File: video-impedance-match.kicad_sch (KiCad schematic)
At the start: 7 parts

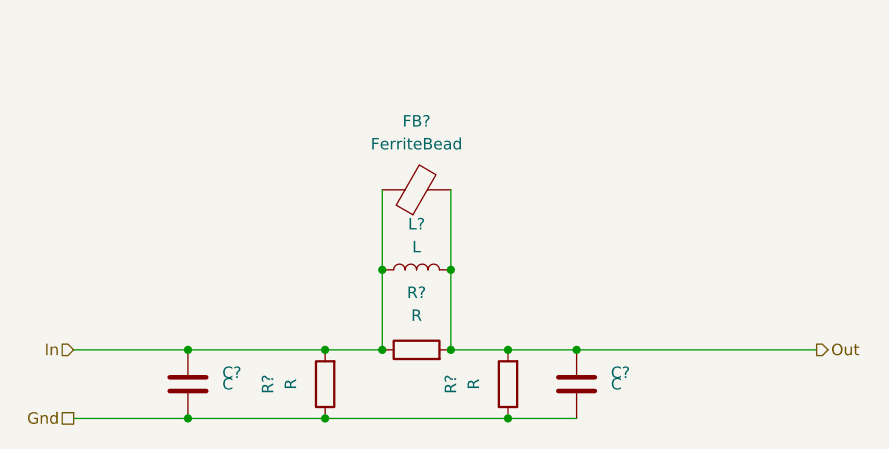
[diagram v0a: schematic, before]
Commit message: Jamma symbol and footprint added. Power supply caps added to schematic.
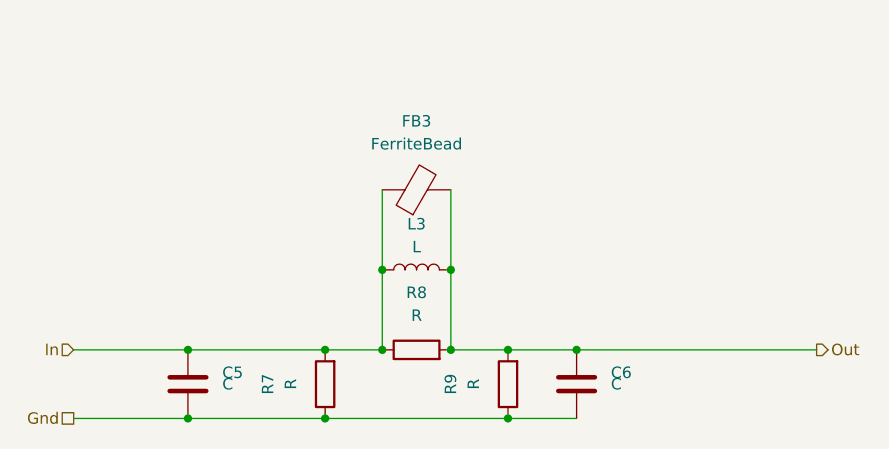
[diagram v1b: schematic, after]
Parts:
- gave numbers to parts that had none: 7
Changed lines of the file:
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@@
   (symbol (lib_id "Device:L") (at 114.3 72.39 90)
     (in_bom yes) (on_board yes)
-    (property "Reference" "L?" (id 0) (at 114.3 67.31 90))
+    (property "Reference" "L3" (id 0) (at 114.3 67.31 90))
     (property "Value" "L" (id 1) (at 114.3 69.85 90))
     (property "Footprint" "" (id 2) (at 114.3 72.39 0)
@@
   (symbol (lib_id "Device:R") (at 104.14 85.09 180)
     (in_bom yes) (on_board yes)
-    (property "Reference" "R?" (id 0) (at 97.79 85.09 90))
+    (property "Reference" "R7" (id 0) (at 97.79 85.09 90))
     (property "Value" "R" (id 1) (at 100.33 85.09 90))
     (property "Footprint" "" (id 2) (at 105.918 85.09 90)
@@
   (symbol (lib_id "Device:R") (at 114.3 81.28 90)
     (in_bom yes) (on_board yes)
-    (property "Reference" "R?" (id 0) (at 114.3 74.93 90))
+    (property "Reference" "R8" (id 0) (at 114.3 74.93 90))
     (property "Value" "R" (id 1) (at 114.3 77.47 90))
     (property "Footprint" "" (id 2) (at 114.3 83.058 90)
@@
   (symbol (lib_id "Device:R") (at 124.46 85.09 180)
     (in_bom yes) (on_board yes)
-    (property "Reference" "R?" (id 0) (at 118.11 85.09 90))
+    (property "Reference" "R9" (id 0) (at 118.11 85.09 90))
     (property "Value" "R" (id 1) (at 120.65 85.09 90))
     (property "Footprint" "" (id 2) (at 126.238 85.09 90)
@@
   (symbol (lib_id "Device:C") (at 88.9 85.09 0)
     (in_bom yes) (on_board yes)
-    (property "Reference" "C?" (id 0) (at 92.71 83.82 0)
+    (property "Reference" "C5" (id 0) (at 92.71 83.82 0)
       (effects (font (size 1.27 1.27)) (justify left))
     )
@@
   (symbol (lib_id "Device:C") (at 132.08 85.09 0)
     (in_bom yes) (on_board yes)
-    (property "Reference" "C?" (id 0) (at 135.89 83.82 0)
+    (property "Reference" "C6" (id 0) (at 135.89 83.82 0)
       (effects (font (size 1.27 1.27)) (justify left))
     )
@@
   (symbol (lib_id "Device:FerriteBead") (at 114.3 63.5 90)
     (in_bom yes) (on_board yes)
-    (property "Reference" "FB?" (id 0) (at 114.3 55.88 90))
+    (property "Reference" "FB3" (id 0) (at 114.3 55.88 90))
     (property "Value" "FerriteBead" (id 1) (at 114.3 58.42 90))
     (property "Footprint" "" (id 2) (at 114.3 65.278 90)

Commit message: Progress with labels and footprints
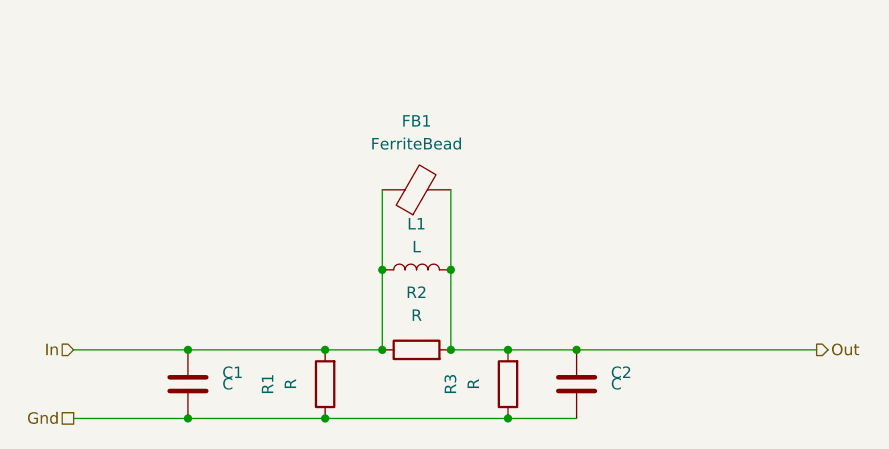
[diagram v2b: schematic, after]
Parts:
- C1: renamed from C5; footprint (none) -> Capacitor_SMD:C_0603_1608Metric
- C2: renamed from C6; footprint (none) -> Capacitor_SMD:C_0603_1608Metric
- FB1: renamed from FB3; footprint (none) -> Resistor_SMD:R_0603_1608Metric
- L1: renamed from L3; footprint (none) -> Resistor_SMD:R_1210_3225Metric
- R1: renamed from R7; footprint (none) -> Resistor_SMD:R_0603_1608Metric
- R2: renamed from R8; footprint (none) -> Resistor_SMD:R_0603_1608Metric
- R3: renamed from R9; footprint (none) -> Resistor_SMD:R_0603_1608Metric
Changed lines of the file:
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@@
   (symbol (lib_id "Device:L") (at 114.3 72.39 90)
     (in_bom yes) (on_board yes)
-    (property "Reference" "L3" (id 0) (at 114.3 67.31 90))
+    (property "Reference" "L1" (id 0) (at 114.3 67.31 90))
     (property "Value" "L" (id 1) (at 114.3 69.85 90))
-    (property "Footprint" "" (id 2) (at 114.3 72.39 0)
+    (property "Footprint" "Resistor_SMD:R_1210_3225Metric" (id 2) (at 114.3 72.39 0)
       (effects (font (size 1.27 1.27)) hide)
     )
@@
   (symbol (lib_id "Device:R") (at 104.14 85.09 180)
     (in_bom yes) (on_board yes)
-    (property "Reference" "R7" (id 0) (at 97.79 85.09 90))
+    (property "Reference" "R1" (id 0) (at 97.79 85.09 90))
     (property "Value" "R" (id 1) (at 100.33 85.09 90))
-    (property "Footprint" "" (id 2) (at 105.918 85.09 90)
+    (property "Footprint" "Resistor_SMD:R_0603_1608Metric" (id 2) (at 105.918 85.09 90)
       (effects (font (size 1.27 1.27)) hide)
     )
@@
   (symbol (lib_id "Device:R") (at 114.3 81.28 90)
     (in_bom yes) (on_board yes)
-    (property "Reference" "R8" (id 0) (at 114.3 74.93 90))
+    (property "Reference" "R2" (id 0) (at 114.3 74.93 90))
     (property "Value" "R" (id 1) (at 114.3 77.47 90))
-    (property "Footprint" "" (id 2) (at 114.3 83.058 90)
+    (property "Footprint" "Resistor_SMD:R_0603_1608Metric" (id 2) (at 114.3 83.058 90)
       (effects (font (size 1.27 1.27)) hide)
     )
@@
   (symbol (lib_id "Device:R") (at 124.46 85.09 180)
     (in_bom yes) (on_board yes)
-    (property "Reference" "R9" (id 0) (at 118.11 85.09 90))
+    (property "Reference" "R3" (id 0) (at 118.11 85.09 90))
     (property "Value" "R" (id 1) (at 120.65 85.09 90))
-    (property "Footprint" "" (id 2) (at 126.238 85.09 90)
+    (property "Footprint" "Resistor_SMD:R_0603_1608Metric" (id 2) (at 126.238 85.09 90)
       (effects (font (size 1.27 1.27)) hide)
     )
@@
   (symbol (lib_id "Device:C") (at 88.9 85.09 0)
     (in_bom yes) (on_board yes)
-    (property "Reference" "C5" (id 0) (at 92.71 83.82 0)
+    (property "Reference" "C1" (id 0) (at 92.71 83.82 0)
       (effects (font (size 1.27 1.27)) (justify left))
     )
@@
       (effects (font (size 1.27 1.27)) (justify left))
     )
-    (property "Footprint" "" (id 2) (at 89.8652 88.9 0)
+    (property "Footprint" "Capacitor_SMD:C_0603_1608Metric" (id 2) (at 89.8652 88.9 0)
       (effects (font (size 1.27 1.27)) hide)
     )
@@
   (symbol (lib_id "Device:C") (at 132.08 85.09 0)
     (in_bom yes) (on_board yes)
-    (property "Reference" "C6" (id 0) (at 135.89 83.82 0)
+    (property "Reference" "C2" (id 0) (at 135.89 83.82 0)
       (effects (font (size 1.27 1.27)) (justify left))
     )
@@
       (effects (font (size 1.27 1.27)) (justify left))
     )
-    (property "Footprint" "" (id 2) (at 133.0452 88.9 0)
+    (property "Footprint" "Capacitor_SMD:C_0603_1608Metric" (id 2) (at 133.0452 88.9 0)
       (effects (font (size 1.27 1.27)) hide)
     )
@@
   (symbol (lib_id "Device:FerriteBead") (at 114.3 63.5 90)
     (in_bom yes) (on_board yes)
-    (property "Reference" "FB3" (id 0) (at 114.3 55.88 90))
+    (property "Reference" "FB1" (id 0) (at 114.3 55.88 90))
     (property "Value" "FerriteBead" (id 1) (at 114.3 58.42 90))
-    (property "Footprint" "" (id 2) (at 114.3 65.278 90)
+    (property "Footprint" "Resistor_SMD:R_0603_1608Metric" (id 2) (at 114.3 65.278 90)
       (effects (font (size 1.27 1.27)) hide)
     )

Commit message: Added more power bypassing capacitors to 5v and 12v supplies.
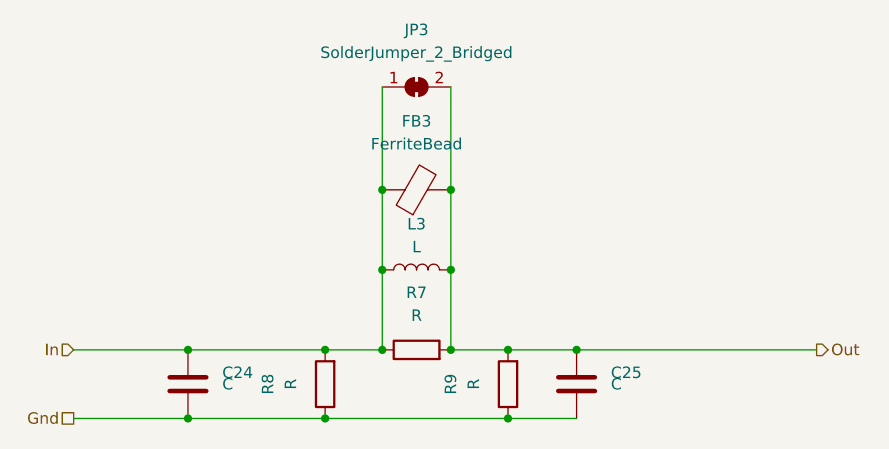
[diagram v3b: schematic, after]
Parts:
- added JP3: SolderJumper_2_Bridged, Jumper:SolderJumper-2_P1.3mm_Bridged_Pad1.0x1.5mm, symbol Jumper:SolderJumper_2_Bridged
- renumbered C1 to C24, C2 to C25, FB1 to FB3, L1 to L3, R2 to R7, R1 to R8, R3 to R9
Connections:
- net In: now also JP3.1 (A)
- net Out: now also JP3.2 (B)
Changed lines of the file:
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@@
   (junction (at 104.14 81.28) (diameter 0.9144) (color 0 0 0 0))
   (junction (at 104.14 88.9) (diameter 0.9144) (color 0 0 0 0))
+  (junction (at 110.49 63.5) (diameter 0.9144) (color 0 0 0 0))
   (junction (at 110.49 72.39) (diameter 0.9144) (color 0 0 0 0))
   (junction (at 110.49 81.28) (diameter 0.9144) (color 0 0 0 0))
+  (junction (at 118.11 63.5) (diameter 0.9144) (color 0 0 0 0))
   (junction (at 118.11 72.39) (diameter 0.9144) (color 0 0 0 0))
   (junction (at 118.11 81.28) (diameter 0.9144) (color 0 0 0 0))
@@
     (stroke (width 0) (type solid) (color 0 0 0 0))
   )
+  (wire (pts (xy 110.49 52.07) (xy 110.49 63.5))
+    (stroke (width 0) (type solid) (color 0 0 0 0))
+  )
   (wire (pts (xy 110.49 63.5) (xy 110.49 72.39))
     (stroke (width 0) (type solid) (color 0 0 0 0))
   )
   (wire (pts (xy 110.49 72.39) (xy 110.49 81.28))
+    (stroke (width 0) (type solid) (color 0 0 0 0))
+  )
+  (wire (pts (xy 118.11 52.07) (xy 118.11 63.5))
     (stroke (width 0) (type solid) (color 0 0 0 0))
   )
@@
   (symbol (lib_id "Device:L") (at 114.3 72.39 90)
     (in_bom yes) (on_board yes)
-    (property "Reference" "L1" (id 0) (at 114.3 67.31 90))
+    (property "Reference" "L3" (id 0) (at 114.3 67.31 90))
     (property "Value" "L" (id 1) (at 114.3 69.85 90))
     (property "Footprint" "Resistor_SMD:R_1210_3225Metric" (id 2) (at 114.3 72.39 0)
@@
   (symbol (lib_id "Device:R") (at 104.14 85.09 180)
     (in_bom yes) (on_board yes)
-    (property "Reference" "R1" (id 0) (at 97.79 85.09 90))
+    (property "Reference" "R8" (id 0) (at 97.79 85.09 90))
     (property "Value" "R" (id 1) (at 100.33 85.09 90))
     (property "Footprint" "Resistor_SMD:R_0603_1608Metric" (id 2) (at 105.918 85.09 90)
@@
   (symbol (lib_id "Device:R") (at 114.3 81.28 90)
     (in_bom yes) (on_board yes)
-    (property "Reference" "R2" (id 0) (at 114.3 74.93 90))
+    (property "Reference" "R7" (id 0) (at 114.3 74.93 90))
     (property "Value" "R" (id 1) (at 114.3 77.47 90))
     (property "Footprint" "Resistor_SMD:R_0603_1608Metric" (id 2) (at 114.3 83.058 90)
@@
   (symbol (lib_id "Device:R") (at 124.46 85.09 180)
     (in_bom yes) (on_board yes)
-    (property "Reference" "R3" (id 0) (at 118.11 85.09 90))
+    (property "Reference" "R9" (id 0) (at 118.11 85.09 90))
     (property "Value" "R" (id 1) (at 120.65 85.09 90))
     (property "Footprint" "Resistor_SMD:R_0603_1608Metric" (id 2) (at 126.238 85.09 90)
@@
     )
   )
+  (symbol (lib_id "Jumper:SolderJumper_2_Bridged") (at 114.3 52.07 0)
+    (in_bom yes) (on_board yes)
+    (property "Reference" "JP3" (id 0) (at 114.3 45.72 0))
+    (property "Value" "SolderJumper_2_Bridged" (id 1) (at 114.3 48.26 0))
+    (property "Footprint" "Jumper:SolderJumper-2_P1.3mm_Bridged_Pad1.0x1.5mm" (id 2) (at 114.3 52.07 0)
+      (effects (font (size 1.27 1.27)) hide)
+    )
+    (property "Datasheet" "~" (id 3) (at 114.3 52.07 0)
+      (effects (font (size 1.27 1.27)) hide)
+    )
+  )
   (symbol (lib_id "Device:C") (at 88.9 85.09 0)
     (in_bom yes) (on_board yes)
-    (property "Reference" "C1" (id 0) (at 92.71 83.82 0)
+    (property "Reference" "C24" (id 0) (at 92.71 83.82 0)
       (effects (font (size 1.27 1.27)) (justify left))
     )
@@
   (symbol (lib_id "Device:C") (at 132.08 85.09 0)
     (in_bom yes) (on_board yes)
-    (property "Reference" "C2" (id 0) (at 135.89 83.82 0)
+    (property "Reference" "C25" (id 0) (at 135.89 83.82 0)
       (effects (font (size 1.27 1.27)) (justify left))
     )
@@
   (symbol (lib_id "Device:FerriteBead") (at 114.3 63.5 90)
     (in_bom yes) (on_board yes)
-    (property "Reference" "FB1" (id 0) (at 114.3 55.88 90))
+    (property "Reference" "FB3" (id 0) (at 114.3 55.88 90))
     (property "Value" "FerriteBead" (id 1) (at 114.3 58.42 90))
     (property "Footprint" "Resistor_SMD:R_0603_1608Metric" (id 2) (at 114.3 65.278 90)

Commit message: Added test points/breakout points for video filter input and output
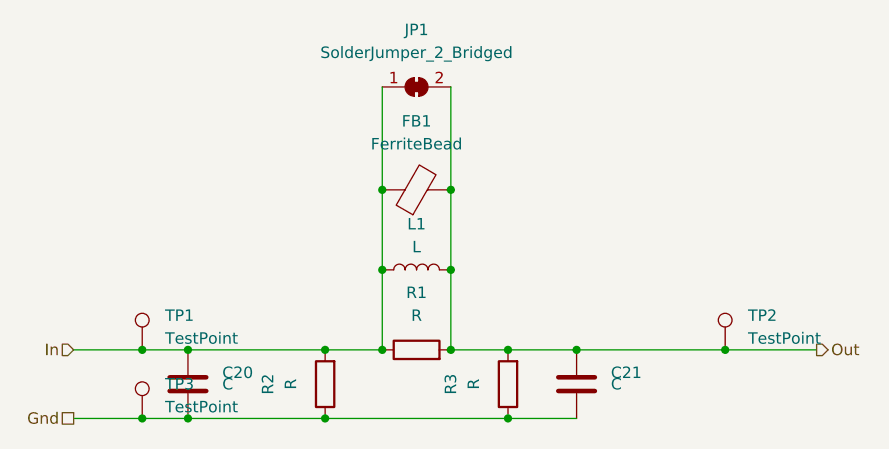
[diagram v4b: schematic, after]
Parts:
- added TP1, TP2, TP3: TestPoint, Connector_PinHeader_2.54mm:PinHeader_1x01_P2.54mm_Vertical, symbol Connector:TestPoint
- renumbered C24 to C20, C25 to C21, FB3 to FB1, JP3 to JP1, L3 to L1, R7 to R1, R8 to R2, R9 to R3
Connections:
- net Gnd: now also TP3.1
- net In: now also TP1.1
- net Out: now also TP2.1
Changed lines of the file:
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@@
   (page 0 4)
   (paper "A4")
+  (junction (at 83.82 81.28) (diameter 0.9144) (color 0 0 0 0))
+  (junction (at 83.82 88.9) (diameter 0.9144) (color 0 0 0 0))
   (junction (at 88.9 81.28) (diameter 0.9144) (color 0 0 0 0))
   (junction (at 88.9 88.9) (diameter 0.9144) (color 0 0 0 0))
@@
   (junction (at 124.46 88.9) (diameter 0.9144) (color 0 0 0 0))
   (junction (at 132.08 81.28) (diameter 0.9144) (color 0 0 0 0))
-  (wire (pts (xy 76.2 81.28) (xy 88.9 81.28))
-    (stroke (width 0) (type solid) (color 0 0 0 0))
-  )
-  (wire (pts (xy 76.2 88.9) (xy 88.9 88.9))
+  (junction (at 148.59 81.28) (diameter 0.9144) (color 0 0 0 0))
+  (wire (pts (xy 76.2 81.28) (xy 83.82 81.28))
+    (stroke (width 0) (type solid) (color 0 0 0 0))
+  )
+  (wire (pts (xy 76.2 88.9) (xy 83.82 88.9))
+    (stroke (width 0) (type solid) (color 0 0 0 0))
+  )
+  (wire (pts (xy 83.82 81.28) (xy 88.9 81.28))
+    (stroke (width 0) (type solid) (color 0 0 0 0))
+  )
+  (wire (pts (xy 83.82 88.9) (xy 88.9 88.9))
     (stroke (width 0) (type solid) (color 0 0 0 0))
   )
@@
     (stroke (width 0) (type solid) (color 0 0 0 0))
   )
-  (wire (pts (xy 132.08 81.28) (xy 158.75 81.28))
+  (wire (pts (xy 132.08 81.28) (xy 148.59 81.28))
+    (stroke (width 0) (type solid) (color 0 0 0 0))
+  )
+  (wire (pts (xy 148.59 81.28) (xy 158.75 81.28))
     (stroke (width 0) (type solid) (color 0 0 0 0))
   )
@@
     (effects (font (size 1.27 1.27)) (justify left))
   )
+  (symbol (lib_id "Connector:TestPoint") (at 83.82 81.28 0)
+    (in_bom yes) (on_board yes)
+    (property "Reference" "TP1" (id 0) (at 86.36 77.47 0)
+      (effects (font (size 1.27 1.27)) (justify left))
+    )
+    (property "Value" "TestPoint" (id 1) (at 86.36 80.01 0)
+      (effects (font (size 1.27 1.27)) (justify left))
+    )
+    (property "Footprint" "Connector_PinHeader_2.54mm:PinHeader_1x01_P2.54mm_Vertical" (id 2) (at 88.9 81.28 0)
+      (effects (font (size 1.27 1.27)) hide)
+    )
+    (property "Datasheet" "~" (id 3) (at 88.9 81.28 0)
+      (effects (font (size 1.27 1.27)) hide)
+    )
+  )
+  (symbol (lib_id "Connector:TestPoint") (at 83.82 88.9 0)
+    (in_bom yes) (on_board yes)
+    (property "Reference" "TP3" (id 0) (at 86.36 85.09 0)
+      (effects (font (size 1.27 1.27)) (justify left))
+    )
+    (property "Value" "TestPoint" (id 1) (at 86.36 87.63 0)
+      (effects (font (size 1.27 1.27)) (justify left))
+    )
+    (property "Footprint" "Connector_PinHeader_2.54mm:PinHeader_1x01_P2.54mm_Vertical" (id 2) (at 88.9 88.9 0)
+      (effects (font (size 1.27 1.27)) hide)
+    )
+    (property "Datasheet" "~" (id 3) (at 88.9 88.9 0)
+      (effects (font (size 1.27 1.27)) hide)
+    )
+  )
+  (symbol (lib_id "Connector:TestPoint") (at 148.59 81.28 0)
+    (in_bom yes) (on_board yes)
+    (property "Reference" "TP2" (id 0) (at 151.13 77.47 0)
+      (effects (font (size 1.27 1.27)) (justify left))
+    )
+    (property "Value" "TestPoint" (id 1) (at 151.13 80.01 0)
+      (effects (font (size 1.27 1.27)) (justify left))
+    )
+    (property "Footprint" "Connector_PinHeader_2.54mm:PinHeader_1x01_P2.54mm_Vertical" (id 2) (at 153.67 81.28 0)
+      (effects (font (size 1.27 1.27)) hide)
+    )
+    (property "Datasheet" "~" (id 3) (at 153.67 81.28 0)
+      (effects (font (size 1.27 1.27)) hide)
+    )
+  )
   (symbol (lib_id "Device:L") (at 114.3 72.39 90)
     (in_bom yes) (on_board yes)
-    (property "Reference" "L3" (id 0) (at 114.3 67.31 90))
+    (property "Reference" "L1" (id 0) (at 114.3 67.31 90))
     (property "Value" "L" (id 1) (at 114.3 69.85 90))
     (property "Footprint" "Resistor_SMD:R_1210_3225Metric" (id 2) (at 114.3 72.39 0)
@@
   (symbol (lib_id "Device:R") (at 104.14 85.09 180)
     (in_bom yes) (on_board yes)
-    (property "Reference" "R8" (id 0) (at 97.79 85.09 90))
+    (property "Reference" "R2" (id 0) (at 97.79 85.09 90))
     (property "Value" "R" (id 1) (at 100.33 85.09 90))
     (property "Footprint" "Resistor_SMD:R_0603_1608Metric" (id 2) (at 105.918 85.09 90)
@@
   (symbol (lib_id "Device:R") (at 114.3 81.28 90)
     (in_bom yes) (on_board yes)
-    (property "Reference" "R7" (id 0) (at 114.3 74.93 90))
+    (property "Reference" "R1" (id 0) (at 114.3 74.93 90))
     (property "Value" "R" (id 1) (at 114.3 77.47 90))
     (property "Footprint" "Resistor_SMD:R_0603_1608Metric" (id 2) (at 114.3 83.058 90)
@@
   (symbol (lib_id "Device:R") (at 124.46 85.09 180)
     (in_bom yes) (on_board yes)
-    (property "Reference" "R9" (id 0) (at 118.11 85.09 90))
+    (property "Reference" "R3" (id 0) (at 118.11 85.09 90))
     (property "Value" "R" (id 1) (at 120.65 85.09 90))
     (property "Footprint" "Resistor_SMD:R_0603_1608Metric" (id 2) (at 126.238 85.09 90)
@@
   (symbol (lib_id "Jumper:SolderJumper_2_Bridged") (at 114.3 52.07 0)
     (in_bom yes) (on_board yes)
-    (property "Reference" "JP3" (id 0) (at 114.3 45.72 0))
+    (property "Reference" "JP1" (id 0) (at 114.3 45.72 0))
     (property "Value" "SolderJumper_2_Bridged" (id 1) (at 114.3 48.26 0))
     (property "Footprint" "Jumper:SolderJumper-2_P1.3mm_Bridged_Pad1.0x1.5mm" (id 2) (at 114.3 52.07 0)
@@
   (symbol (lib_id "Device:C") (at 88.9 85.09 0)
     (in_bom yes) (on_board yes)
-    (property "Reference" "C24" (id 0) (at 92.71 83.82 0)
+    (property "Reference" "C20" (id 0) (at 92.71 83.82 0)
       (effects (font (size 1.27 1.27)) (justify left))
     )
@@
   (symbol (lib_id "Device:C") (at 132.08 85.09 0)
     (in_bom yes) (on_board yes)
-    (property "Reference" "C25" (id 0) (at 135.89 83.82 0)
+    (property "Reference" "C21" (id 0) (at 135.89 83.82 0)
       (effects (font (size 1.27 1.27)) (justify left))
     )
@@
   (symbol (lib_id "Device:FerriteBead") (at 114.3 63.5 90)
     (in_bom yes) (on_board yes)
-    (property "Reference" "FB3" (id 0) (at 114.3 55.88 90))
+    (property "Reference" "FB1" (id 0) (at 114.3 55.88 90))
     (property "Value" "FerriteBead" (id 1) (at 114.3 58.42 90))
     (property "Footprint" "Resistor_SMD:R_0603_1608Metric" (id 2) (at 114.3 65.278 90)
